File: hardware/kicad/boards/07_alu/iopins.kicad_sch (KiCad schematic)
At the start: 13 parts, among them J1 Conn_01x08_Pin, J10 Conn_01x04_Pin, J11 Conn_01x04_Pin, J12 Conn_01x08_Pin, J13 Conn_01x08_Pin, J2 Conn_01x08_Pin, J3 Conn_01x08_Pin, J4 Conn_01x08_Pin, J5 Conn_01x08_Pin, J6 Conn_01x08_Pin, J7 Conn_01x08_Pin, J8 Conn_01x08_Pin, J9 Conn_01x08_Pin

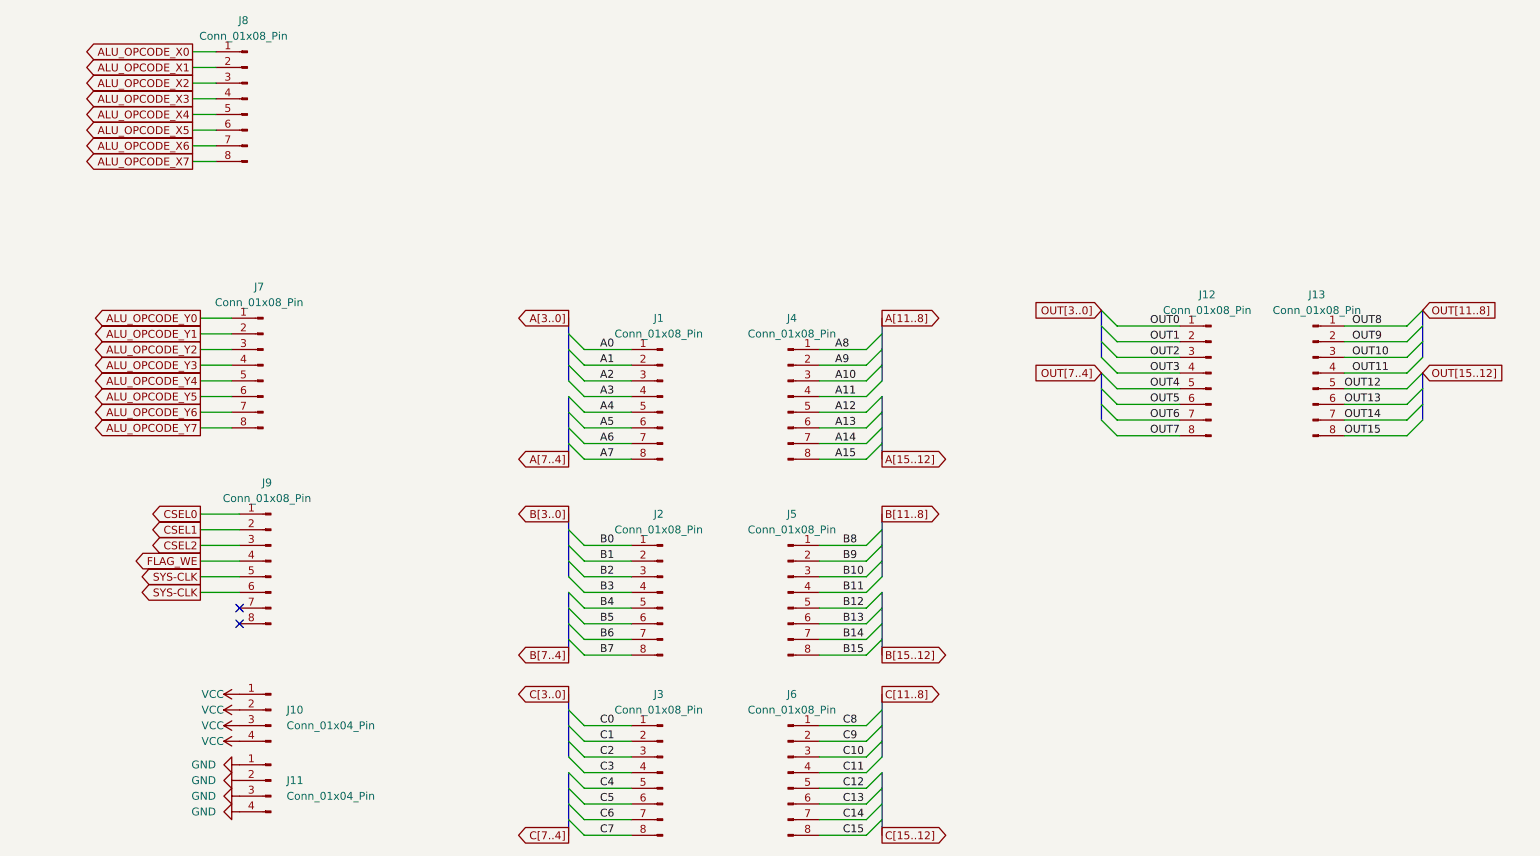
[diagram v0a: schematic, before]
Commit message: fix: resolved kicad erc tests to 0
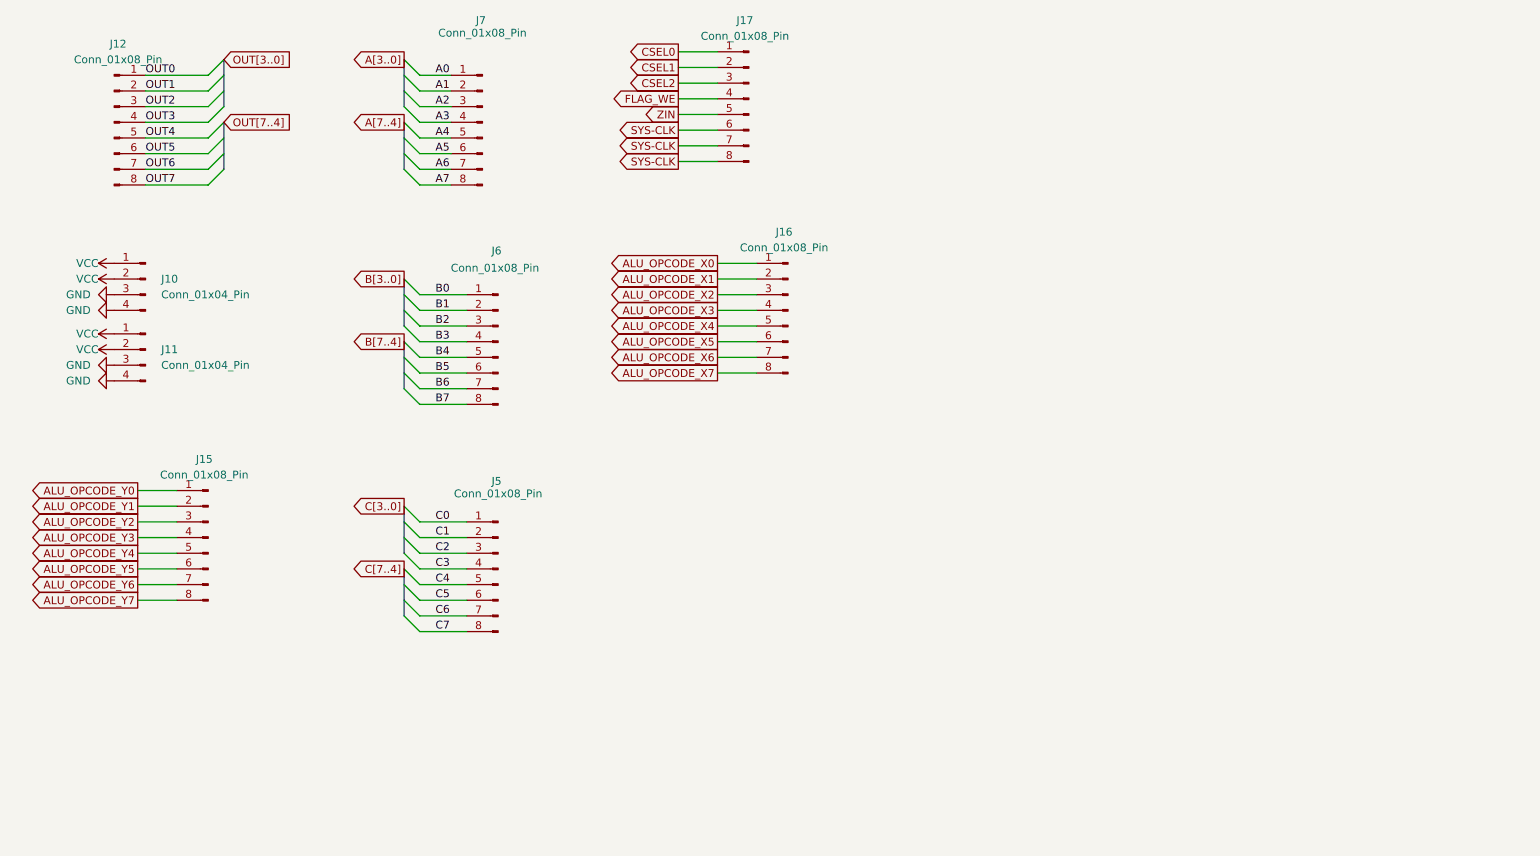
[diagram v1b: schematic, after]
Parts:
- removed J1, J13, J2, J3, J4, J8, J9: Conn_01x08_Pin, Connector_PinHeader_2.54mm:PinHeader_1x08_P2.54mm_Vertical, symbol Connector:Conn_01x08_Pin
- added J15, J16, J17: Conn_01x08_Pin, Connector_PinHeader_2.54mm:PinHeader_1x08_P2.54mm_Vertical, symbol Connector:Conn_01x08_Pin
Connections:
- net B10 is gone; now on net C2: J5.3 (Pin_3)
- net B11 is gone; now on net C3: J5.4 (Pin_4)
- net B12 is gone; now on net C4: J5.5 (Pin_5)
- net B13 is gone; now on net C5: J5.6 (Pin_6)
- net B14 is gone; now on net C6: J5.7 (Pin_7)
- net B15 is gone; now on net C7: J5.8 (Pin_8)
- net B8 is gone; now on net C0: J5.1 (Pin_1)
- net B9 is gone; now on net C1: J5.2 (Pin_2)
- net C10 is gone; now on net B2: J6.3 (Pin_3)
- net C11 is gone; now on net B3: J6.4 (Pin_4)
- net C12 is gone; now on net B4: J6.5 (Pin_5)
- net C13 is gone; now on net B5: J6.6 (Pin_6)
- net C14 is gone; now on net B6: J6.7 (Pin_7)
- net C15 is gone; now on net B7: J6.8 (Pin_8)
- net C8 is gone; now on net B0: J6.1 (Pin_1)
- net C9 is gone; now on net B1: J6.2 (Pin_2)
- net A0: now also J7.1 (Pin_1)
- net A1: now also J7.2 (Pin_2)
- net A2: now also J7.3 (Pin_3)
- net A3: now also J7.4 (Pin_4)
- net A4: now also J7.5 (Pin_5)
- net A5: now also J7.6 (Pin_6)
- net A6: now also J7.7 (Pin_7)
- net A7: now also J7.8 (Pin_8)
- net ALU_OPCODE_X0: now also J16.1 (Pin_1)
- net ALU_OPCODE_X1: now also J16.2 (Pin_2)
- net ALU_OPCODE_X2: now also J16.3 (Pin_3)
- net ALU_OPCODE_X3: now also J16.4 (Pin_4)
- net ALU_OPCODE_X4: now also J16.5 (Pin_5)
- net ALU_OPCODE_X5: now also J16.6 (Pin_6)
- net ALU_OPCODE_X6: now also J16.7 (Pin_7)
- net ALU_OPCODE_X7: now also J16.8 (Pin_8)
- net ALU_OPCODE_Y0: now also J15.1 (Pin_1); no longer J7.1 (Pin_1)
- net ALU_OPCODE_Y1: now also J15.2 (Pin_2); no longer J7.2 (Pin_2)
- net ALU_OPCODE_Y2: now also J15.3 (Pin_3); no longer J7.3 (Pin_3)
- net ALU_OPCODE_Y3: now also J15.4 (Pin_4); no longer J7.4 (Pin_4)
- net ALU_OPCODE_Y4: now also J15.5 (Pin_5); no longer J7.5 (Pin_5)
- net ALU_OPCODE_Y5: now also J15.6 (Pin_6); no longer J7.6 (Pin_6)
- net ALU_OPCODE_Y6: now also J15.7 (Pin_7); no longer J7.7 (Pin_7)
- net ALU_OPCODE_Y7: now also J15.8 (Pin_8); no longer J7.8 (Pin_8)
- net CSEL0: now also J17.1 (Pin_1)
- net CSEL1: now also J17.2 (Pin_2)
- net CSEL2: now also J17.3 (Pin_3)
- net FLAG_WE: now also J17.4 (Pin_4)
- net GND: now also J10.3 (Pin_3), J10.4 (Pin_4); no longer J11.1 (Pin_1), J11.2 (Pin_2)
- net SYS-CLK: now also J17.6 (Pin_6), J17.7 (Pin_7), J17.8 (Pin_8)
- net VCC: now also J11.1 (Pin_1), J11.2 (Pin_2); no longer J10.3 (Pin_3), J10.4 (Pin_4)
- new net ZIN: J17.5 (Pin_5)
- no-connect marks 2 -> 0
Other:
- moved on the sheet: J10, J11, J12

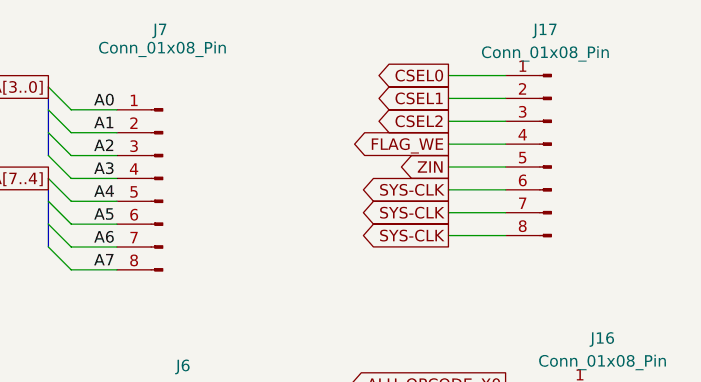
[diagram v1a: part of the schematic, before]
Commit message: checkpoint: routing flags and finishing final traces before pcb annotations and text
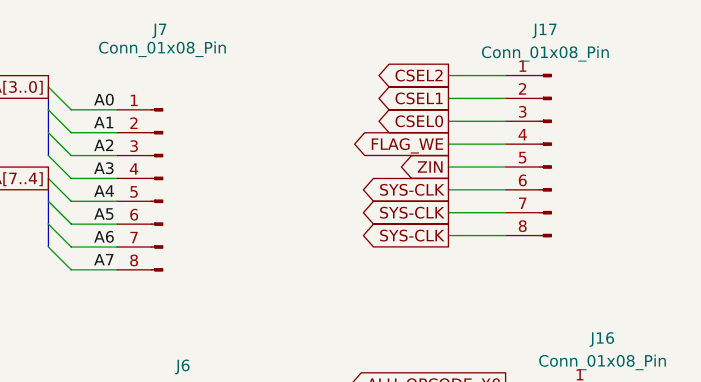
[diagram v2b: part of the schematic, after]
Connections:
- net CSEL0: now also J17.3 (Pin_3); no longer J17.1 (Pin_1)
- net CSEL2: now also J17.1 (Pin_1); no longer J17.3 (Pin_3)
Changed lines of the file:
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@@
 		)
 	)
-	(global_label "CSEL2"
+	(global_label "CSEL0"
 		(shape output)
 		(at 134.62 30.48 180)
@@
 		)
 	)
-	(global_label "CSEL0"
-		(shape output)
-		(at 134.62 25.4 180)
-		(fields_autoplaced yes)
-		(effects
-			(font
-				(size 1.27 1.27)
-			)
-			(justify right)
-		)
-		(property "Intersheetrefs" "${INTERSHEET_REFS}"
-			(at 125.7687 25.4 0)
-			(hide yes)
-			(show_name no)
-			(do_not_autoplace no)
-			(effects
-				(font
-					(size 1.27 1.27)
-				)
-				(justify right)
-			)
-		)
-	)
 	(global_label "ALU_OPCODE_Y1"
 		(shape output)
@@
 			(hide yes)
 			(show_name no)
+			(do_not_autoplace no)
+			(effects
+				(font
+					(size 1.27 1.27)
+				)
+				(justify right)
+			)
+		)
+	)
+	(global_label "CSEL2"
+		(shape output)
+		(at 134.62 25.4 180)
+		(fields_autoplaced yes)
+		(effects
+			(font
+				(size 1.27 1.27)
+			)
+			(justify right)
+		)
+		(property "Intersheetrefs" "${INTERSHEET_REFS}"
+			(at 125.7687 25.4 0)
+			(hide yes)
+			(show_name no)

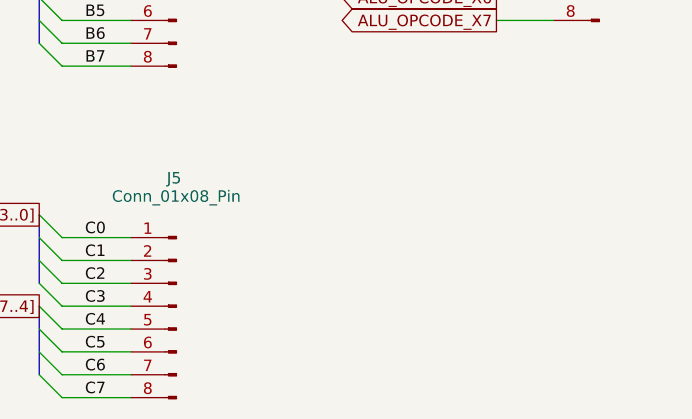
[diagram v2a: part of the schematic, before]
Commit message: fix: placed power flags to resolve flag error in kicad
DRC/ERC are both 0 :)
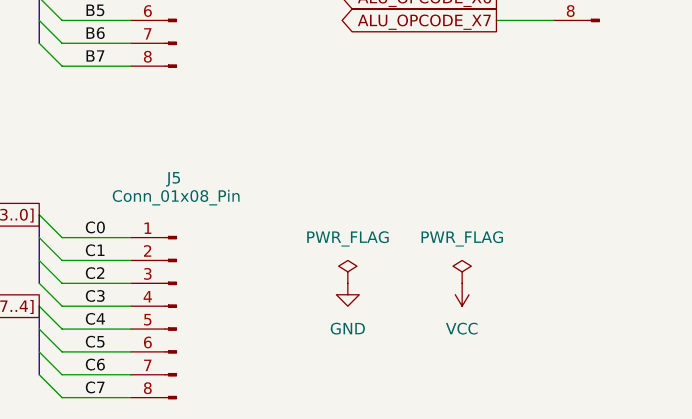
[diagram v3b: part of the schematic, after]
